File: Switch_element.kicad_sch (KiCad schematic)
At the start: 10 parts, among them U601 AP22653AW6-7, U602 AP22653AW6-7

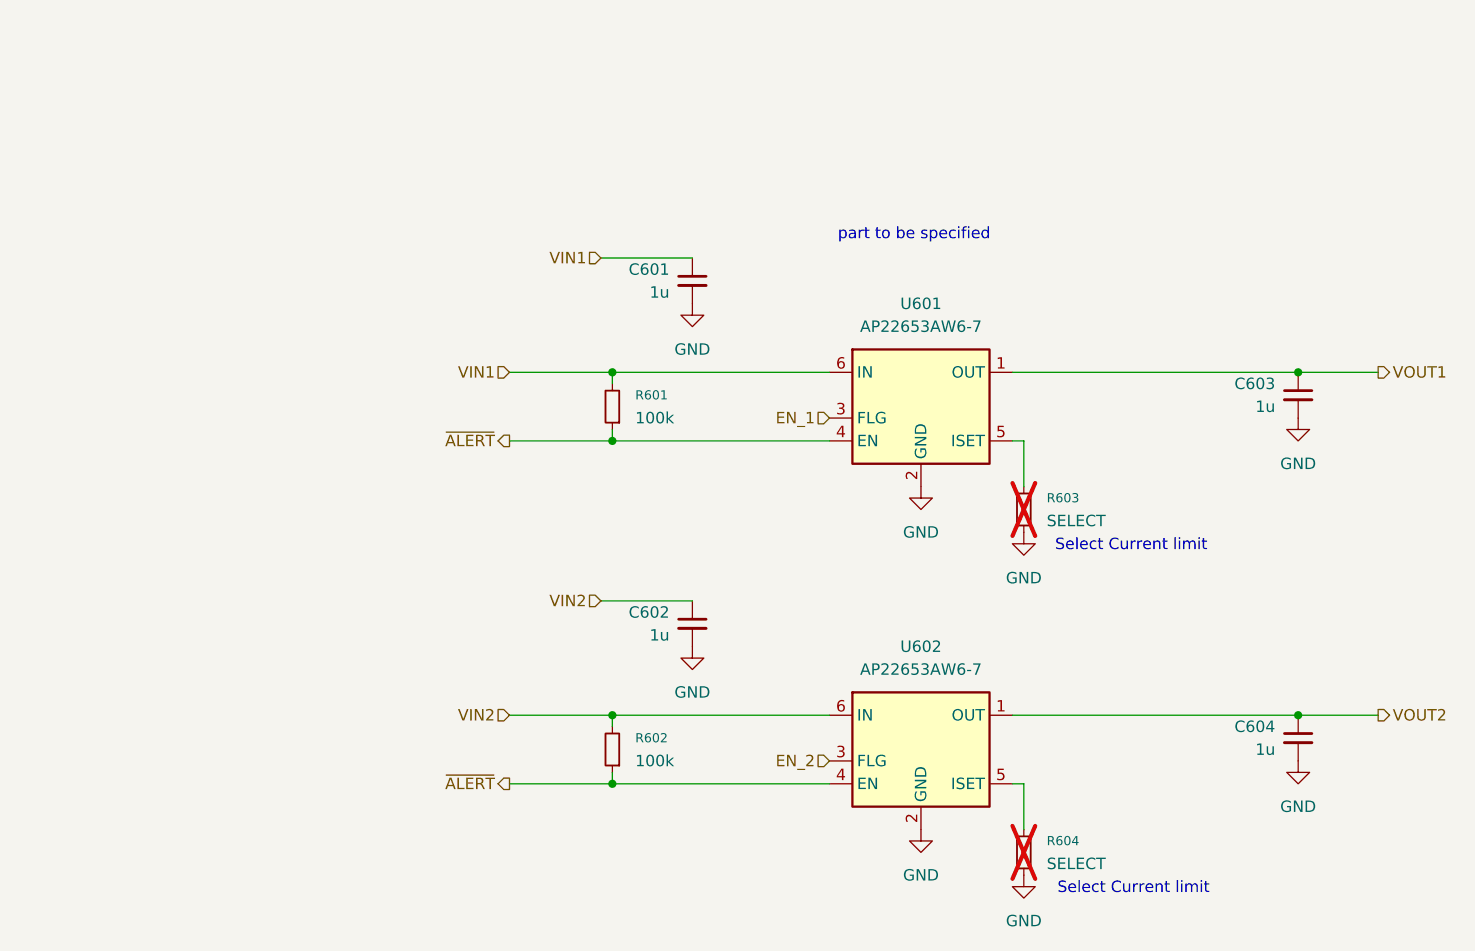
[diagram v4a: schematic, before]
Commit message: wired channel alerts; added schematic for test pbc
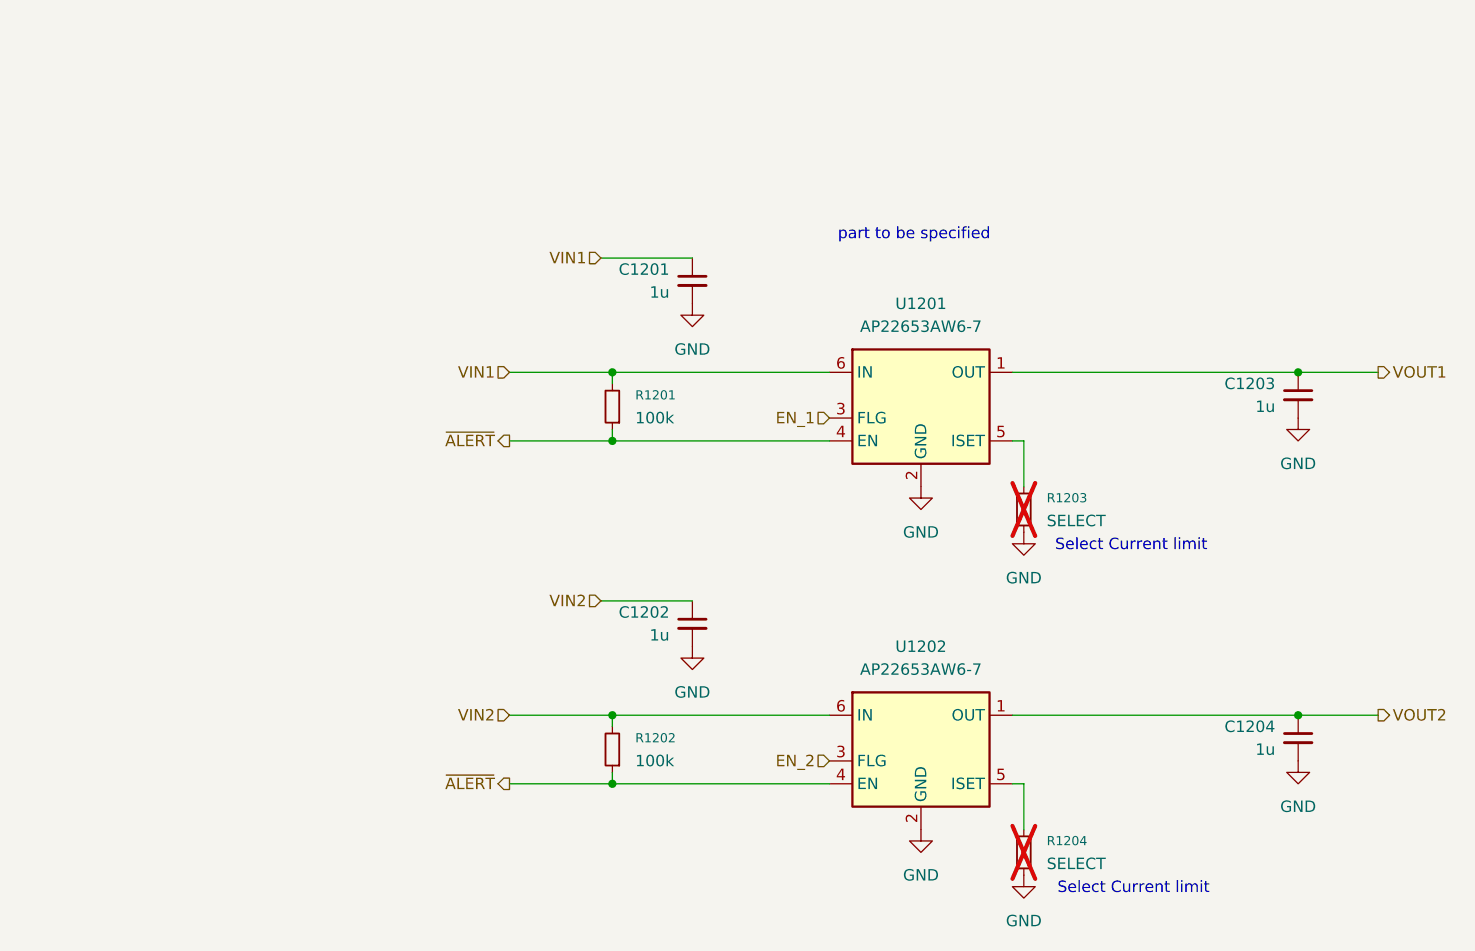
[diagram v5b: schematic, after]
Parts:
- renumbered C601 to C1201, C602 to C1202, C603 to C1203, C604 to C1204, R601 to R1201, R602 to R1202, R603 to R1203, R604 to R1204, U601 to U1201, U602 to U1202

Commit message: reduced number of DCDC converter for PV panels; updated test pcb
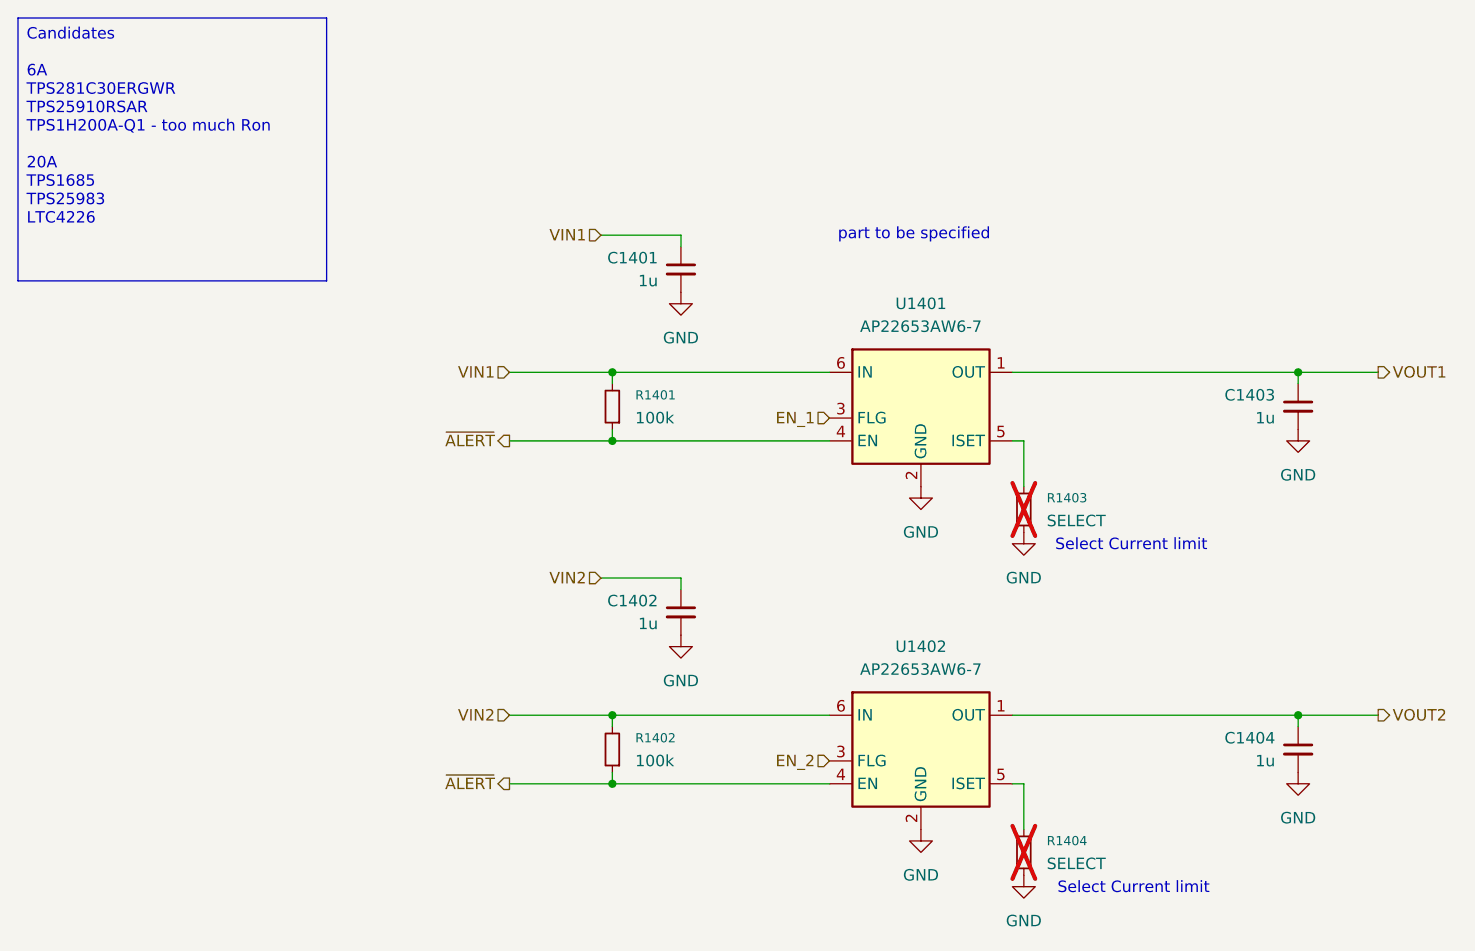
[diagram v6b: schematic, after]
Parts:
- renumbered C1201 to C1401, C1202 to C1402, C1203 to C1403, C1204 to C1404, R1201 to R1401, R1202 to R1402, R1203 to R1403, R1204 to R1404, U1201 to U1401, U1202 to U1402
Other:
- moved on the sheet: C1401, C1402, C1403, C1404

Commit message: added missing heater connectors
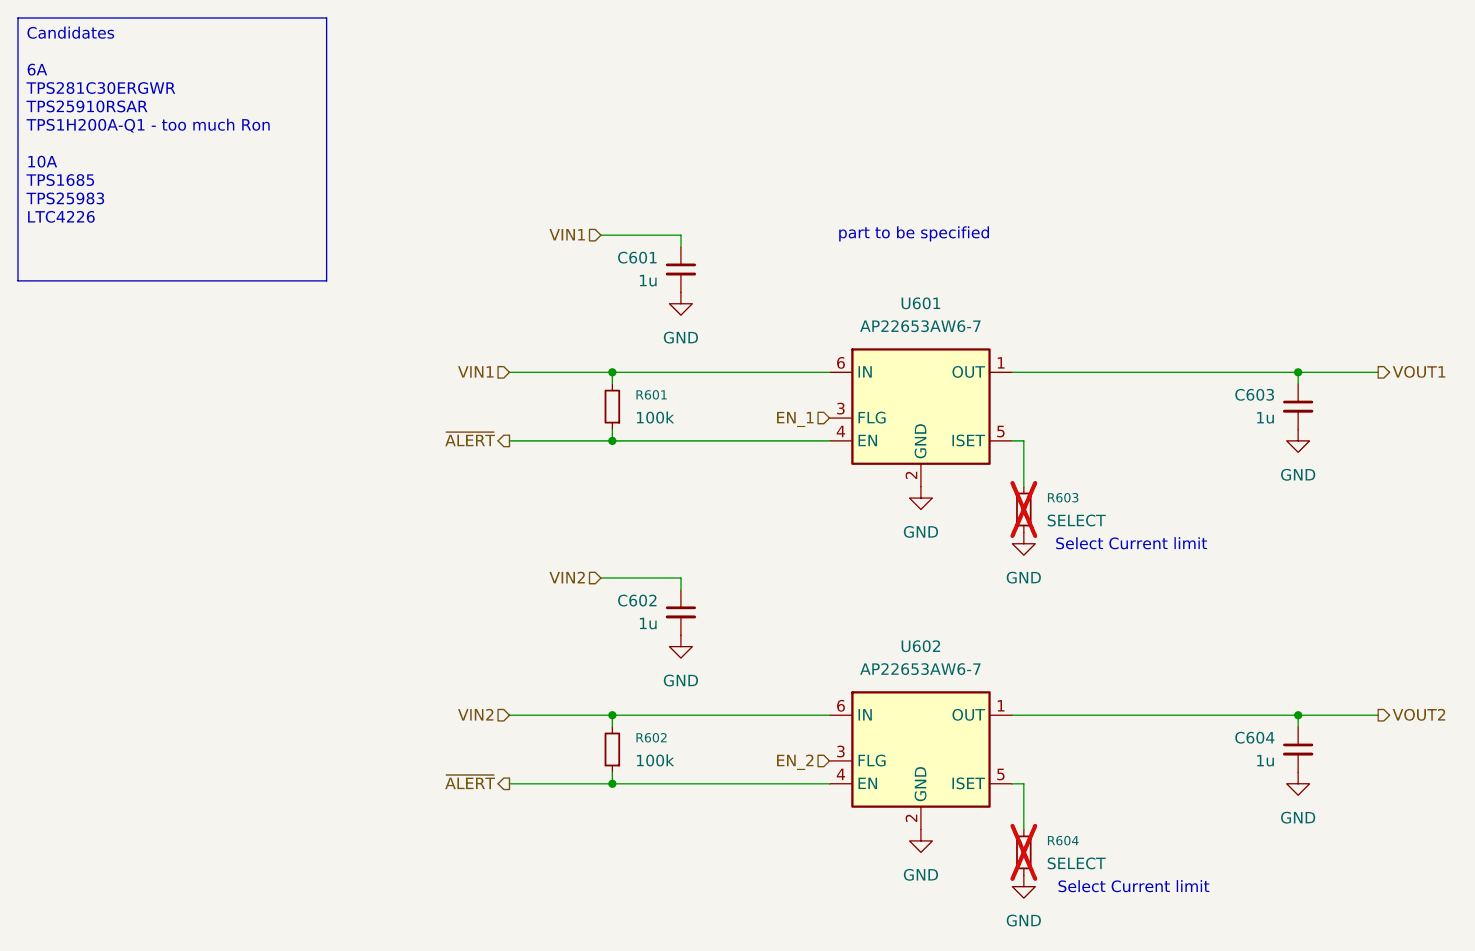
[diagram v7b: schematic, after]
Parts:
- renumbered C1401 to C601, C1402 to C602, C1403 to C603, C1404 to C604, R1401 to R601, R1402 to R602, R1403 to R603, R1404 to R604, U1401 to U601, U1402 to U602
